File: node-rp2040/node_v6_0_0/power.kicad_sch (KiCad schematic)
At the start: 23 parts, among them J10 Connector, USB-TYPE-C-16P, Q1 DMG2301L, U3 AP2112K-3.3, U4 CAT3200-5, U5 MCP73831-2-OT

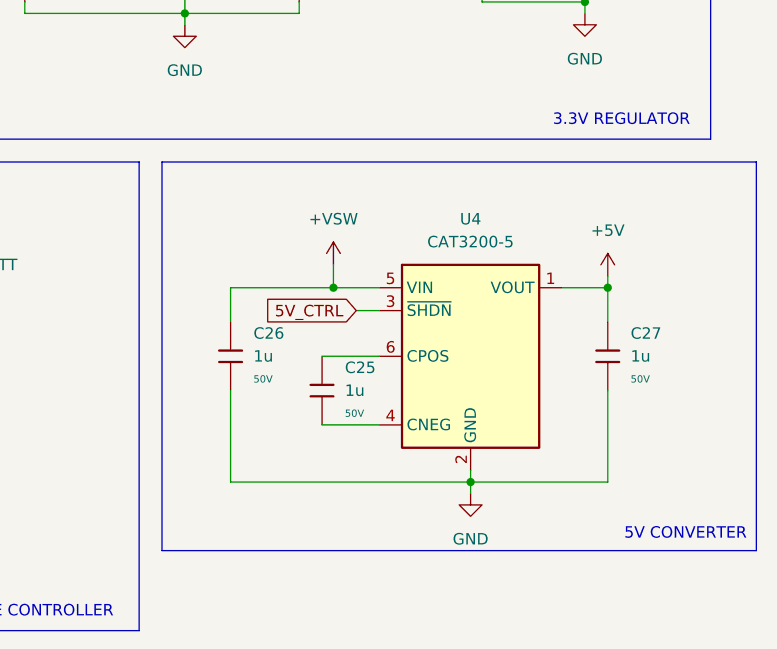
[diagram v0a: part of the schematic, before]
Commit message: i should have made this more than one commit but: 1) started poking around in v5 to find and solve a sim card problem, forgot about it and moved on 2) created v6, modified the schematic somewhat, removed some parts, began laying out the pcb again this time as a 6 layer board 3) fixed the library setup so now it uses symbols and footprints from the packages available alongside kicad (in void linux at least) for all standard stuff PLUS the wisdom libraries and the jlcpcb prefered parts library
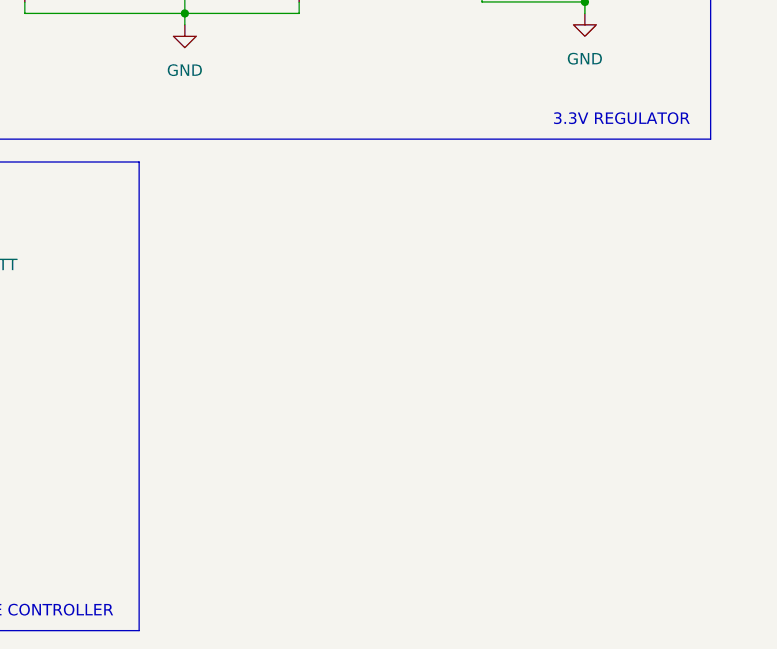
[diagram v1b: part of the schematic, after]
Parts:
- removed C25, C26, C27: 1u, JLCPCB-Kicad-Footprints:C_0805, symbol JLCPCB-Capacitors:0805,1uF
- removed U4: CAT3200-5, Package_TO_SOT_SMD:SOT-23-6, symbol Regulator_SwitchedCapacitor:CAT3200-5
- C21, C22, C23, C24, C39, C40: footprint JLCPCB-Kicad-Footprints:C_0805 -> JLCPCB:C_0805
- D2: footprint JLCPCB-Kicad-Footprints:D_SMA -> JLCPCB:D_SMA
- J10: footprint JLCPCB-Kicad-Footprints:TYPE-C-SMD_HX-TYPE-C-16PIN -> JLCPCB:TYPE-C-SMD_HX-TYPE-C-16PIN
- R17, R18: footprint JLCPCB-Kicad-Footprints:R_0805 -> JLCPCB:R_0805; Stock 213387 -> 196500
- R6, R7, R8: footprint JLCPCB-Kicad-Footprints:R_0805 -> JLCPCB:R_0805
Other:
- note removed: "5V CONVERTER"
